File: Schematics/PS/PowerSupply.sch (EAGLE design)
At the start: 82 parts, among them IC1 LM317MABDT, IC2 LM337, T1 IRFP240, T2 IRFP240

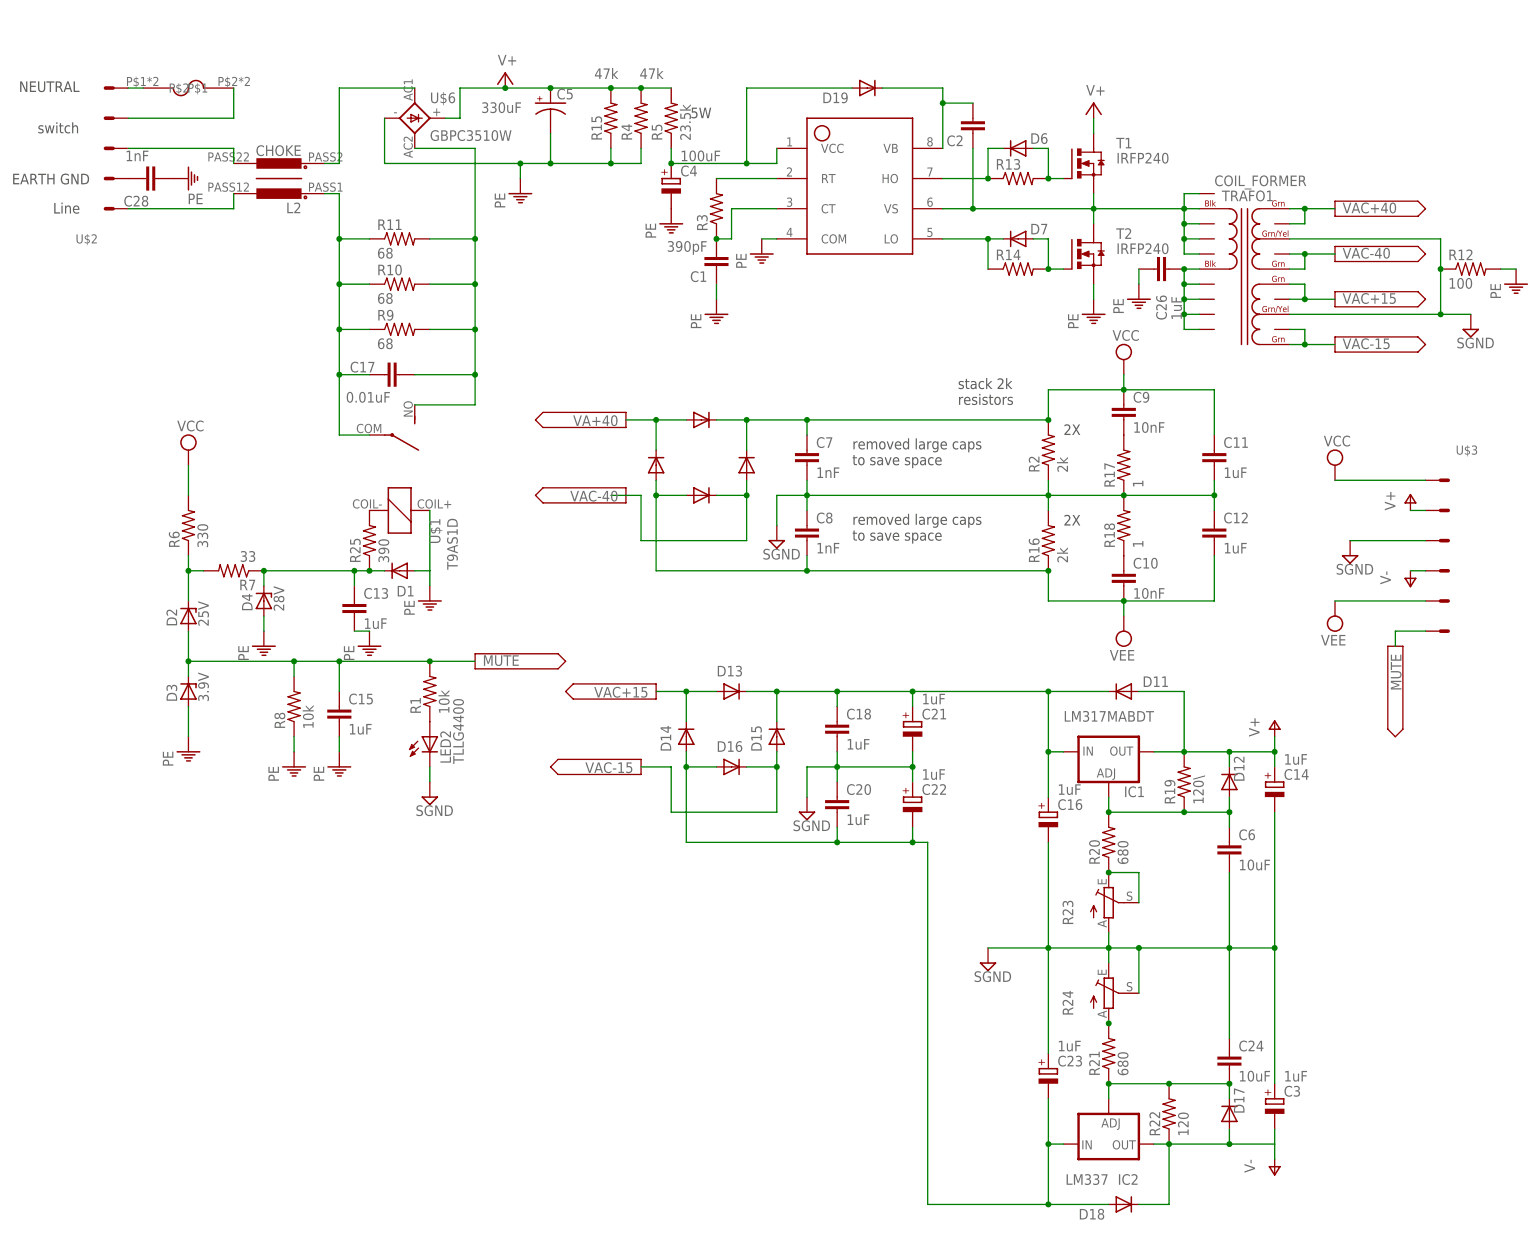
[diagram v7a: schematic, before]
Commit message: updated values on PS board
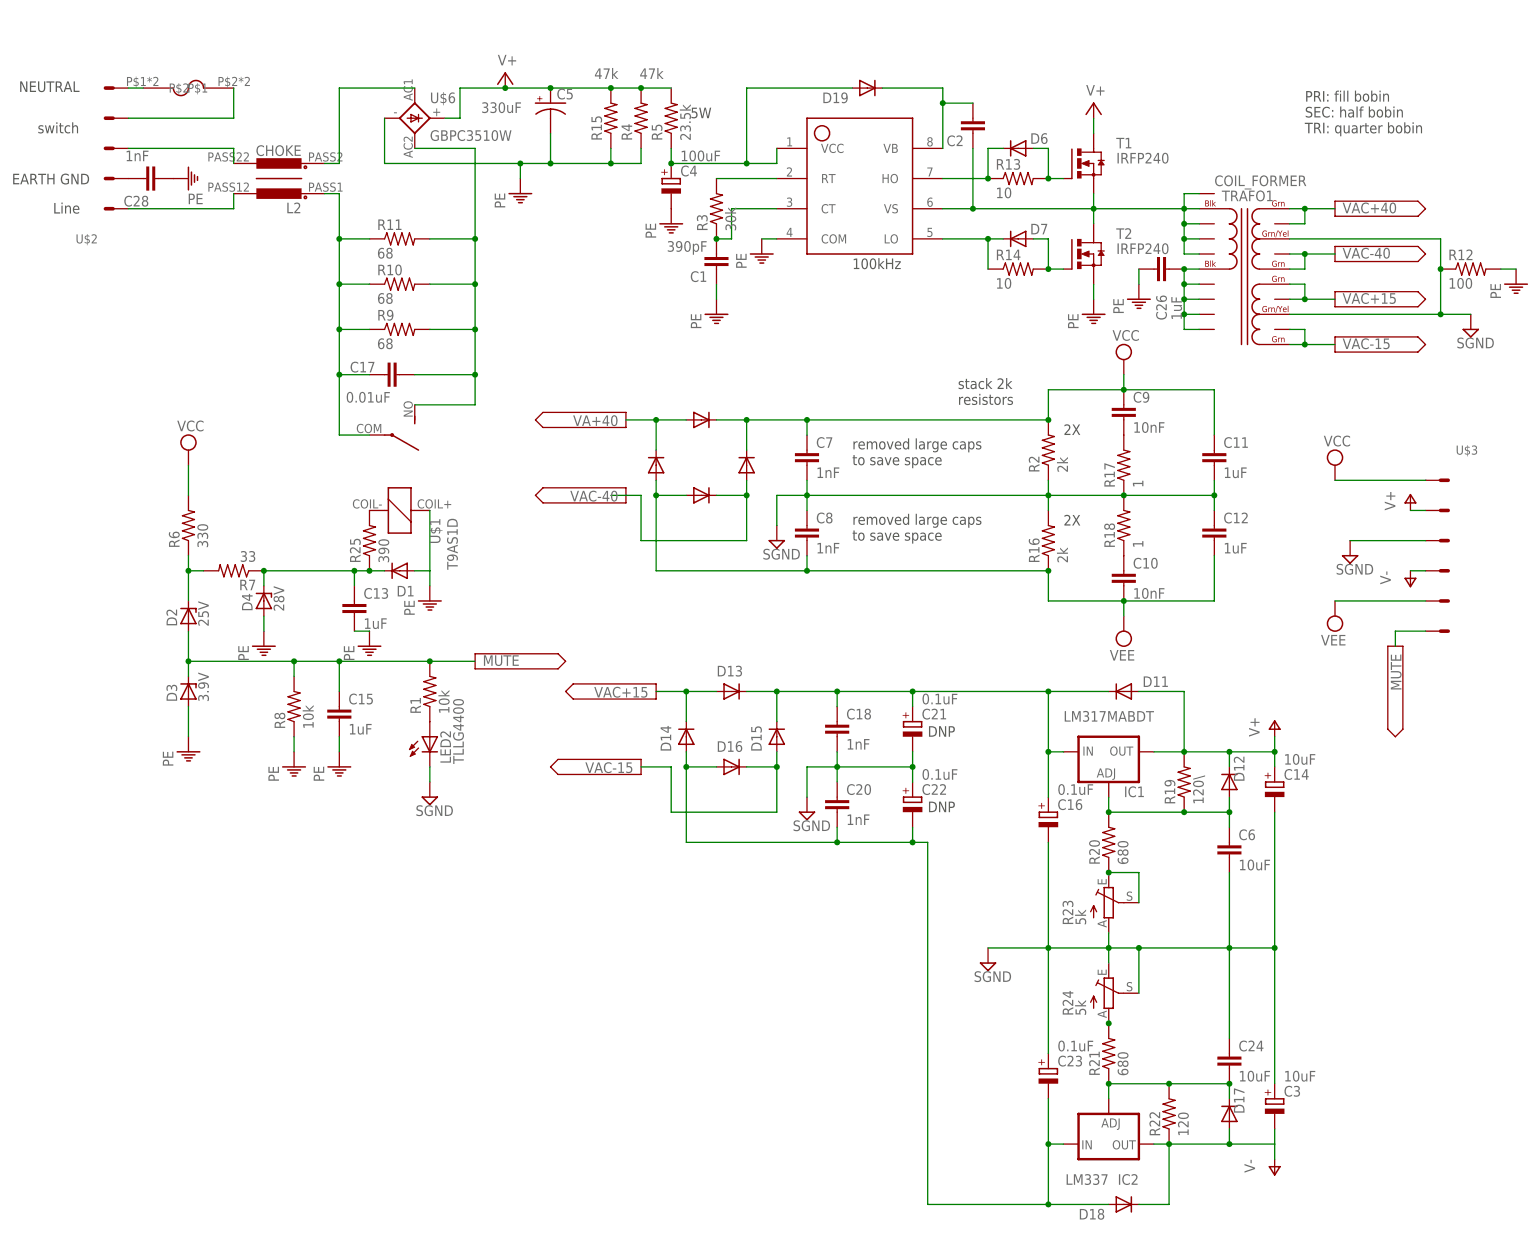
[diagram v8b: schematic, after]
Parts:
- C14, C3: value 1uF -> 10uF
- C16, C21, C22, C23: value 1uF -> 0.1uF
- C18, C20: value 1uF -> 1nF
- R13, R14: value (none) -> 10
- R23, R24: value (none) -> 5k
- R3: value (none) -> 30k
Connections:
- net N$12 renamed SWITCH1
- net N$2 renamed SWITCH2
- net N$5 renamed NUTRAL
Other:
- note added: "100kHz"
- note added: "DNP"
- note added: "PRI: fill bobin SEC: half bobin TRI: quarter bobin"
